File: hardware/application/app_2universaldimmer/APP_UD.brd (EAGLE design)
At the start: 87.1 x 67.3 mm, 94 parts, among them IC102 LM324N, IC2 LM324N, Q1 IRFP460, Q101 IRFP460, Q102 IRFP460, Q103 BC546B, Q104 MPSA44, Q2 IRFP460, Q3 BC546B, Q4 MPSA44

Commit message: Universaldimmer: V2.3 Klemme 101 versetzt
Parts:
- moved KL101 2.54 mm to (5.08, 25.4)
- moved L101 2.54 mm to (8.89, 6.35)
- moved R101 2.54 mm to (8.89, 15.2)
- moved F101 2.22 mm to (3.81, 11.7)
- moved V101 2.22 mm to (2.54, 18.1)
- moved C103 1.27 mm to (2.54, 3.81)
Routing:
- net N$26: track 53.0 -> 50.9 mm
- net N$75: track 17.6 -> 18.8 mm
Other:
- board text added: "2"
- board text added: "24"
- board text added: "25"
- board text added: "8"
- board text added: "9"
- board text added: "Universaldimmer V2.3 Freebus/petzi 15.1.2012"
- board text added: "V2.3"
- board text removed: "Universaldimmer V2.2 Freebus/petzi 5.1.2012"
- board text removed: "V2.2"

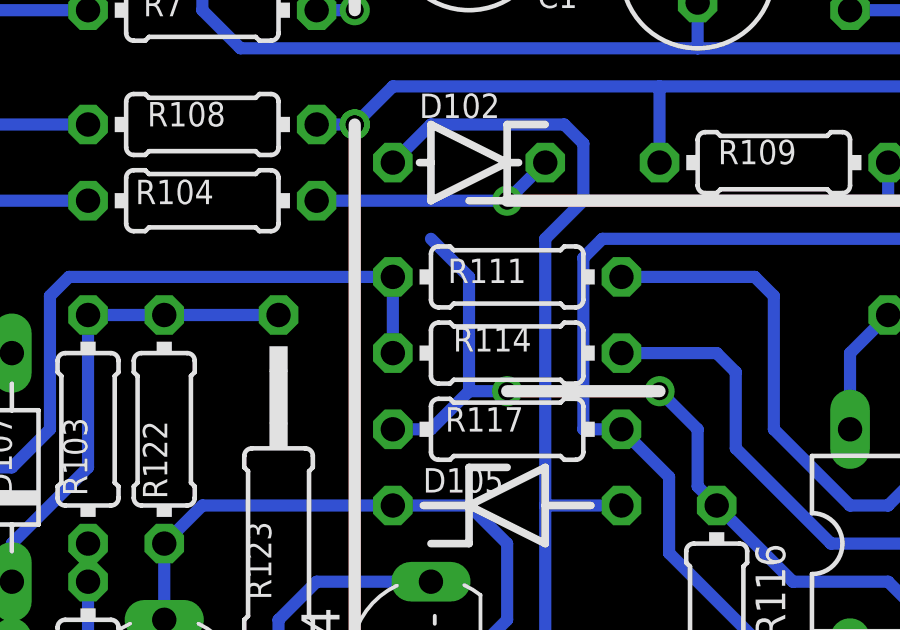
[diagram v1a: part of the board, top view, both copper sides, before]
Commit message: UD: unnötige Leiterbahn entfernt
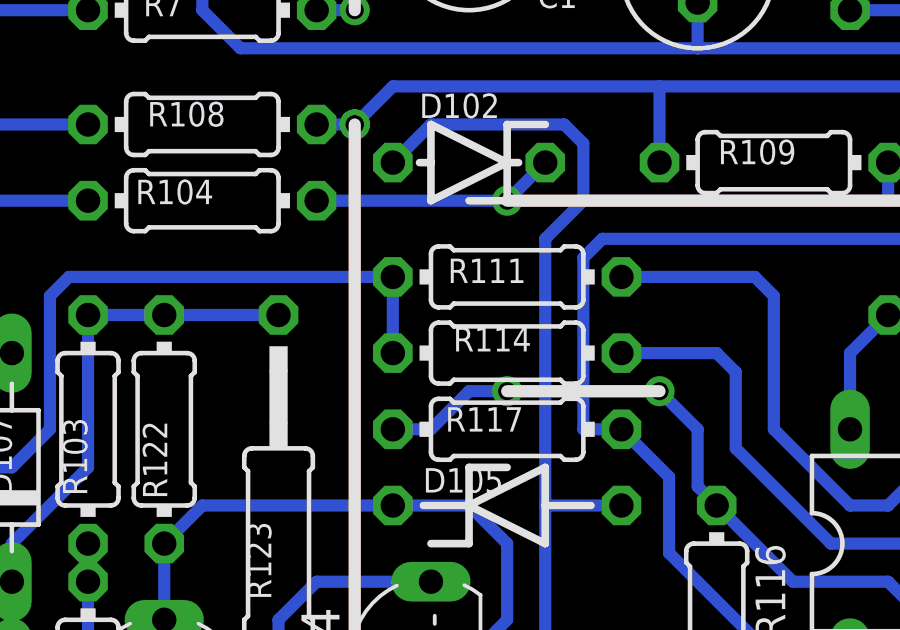
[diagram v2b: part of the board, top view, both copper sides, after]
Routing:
- net N$58: track 29.5 -> 23.8 mm
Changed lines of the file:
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@@
 <contactref element="R117" pad="2"/>
 <contactref element="IC102" pad="2"/>
-<wire x1="31.75" y1="27.94" x2="33.02" y2="26.67" width="0.4064" layer="16"/>
-<wire x1="33.02" y1="26.67" x2="33.02" y2="22.86" width="0.4064" layer="16"/>
 <wire x1="33.02" y1="22.86" x2="31.75" y2="21.59" width="0.4064" layer="16"/>
 <wire x1="31.75" y1="21.59" x2="30.48" y2="21.59" width="0.4064" layer="16"/>

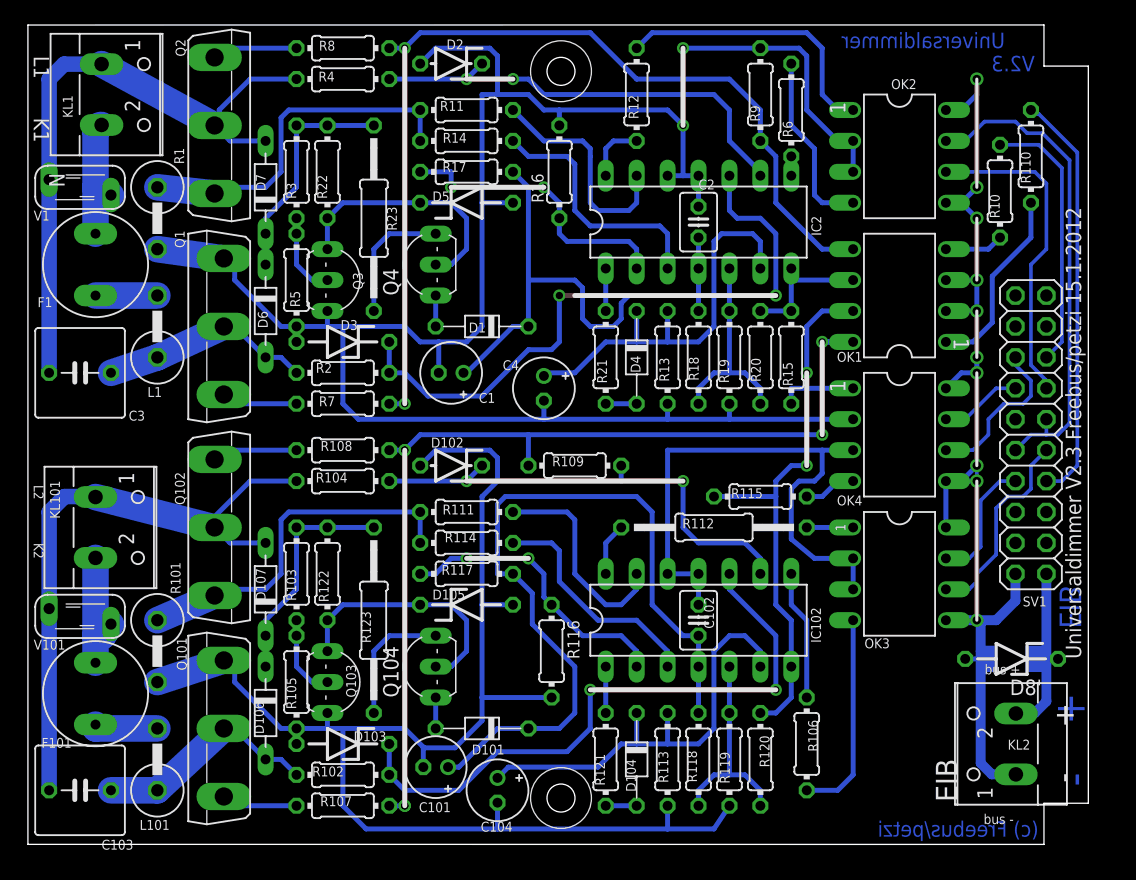
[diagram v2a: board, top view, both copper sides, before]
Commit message: Universaldimmer: V2.4  R23 nun 5Watt,deshalb Layout geändert, Schaltung ist gleich BOM und Warenkorb hinzugefügt
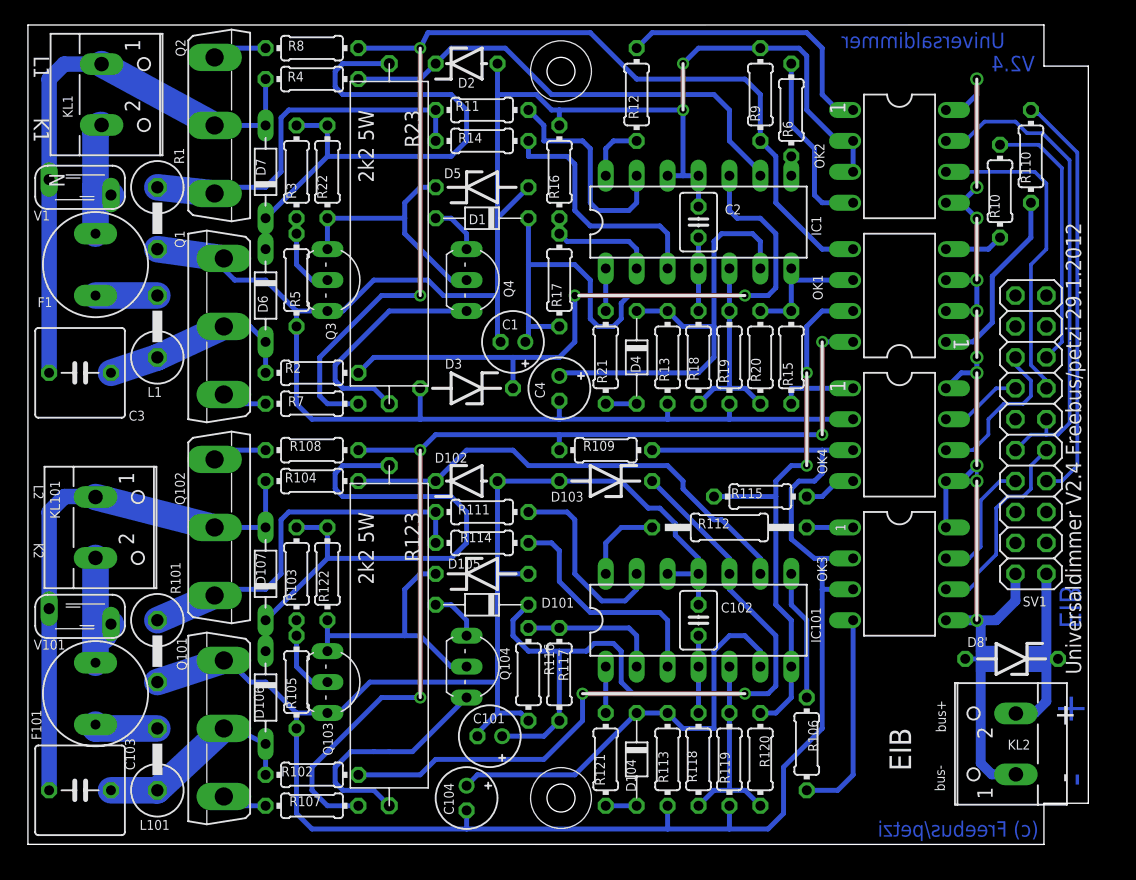
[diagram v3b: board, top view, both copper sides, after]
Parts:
- R109, R9: value 20k -> 22k
- R112: device rcl:0207/15 -> rcl:0207/12
- R123, R23: value 2k2 1W -> 2k2 5W; device rcl:0207/15 -> resistor-power:KH208-8_10B
- moved D103 30.5 mm to (45.7, 29.2)
- moved R17 11.7 mm to (41.9, 45.7), turned to 90 degrees
- moved R117 11.2 mm to (41.9, 13.3), turned to 90 degrees
- moved D3 10.9 mm to (34.3, 36.8)
- moved D101 10.2 mm to (35.6, 19.1)
- moved D1 8.89 mm to (35.6, 50.8)
- moved C1 5.68 mm to (38.1, 40.6)
- moved Q4 5.24 mm to (35.6, 45.7), turned to 270 degrees
- moved C101 5.12 mm to (36.2, 8.26)
- moved Q104 5.08 mm to (35.6, 14.0), turned to 270 degrees
- moved D105 2.84 mm to (35.6, 21.6)
- moved R109 2.84 mm to (45.7, 31.8)
- moved R116 2.69 mm to (39.4, 13.3)
- moved C104 2.62 mm to (34.3, 3.17)
- moved R102 2.54 mm to (21.6, 5.08)
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- renumbered IC102 to IC101, IC2 to IC1
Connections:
- net N$12: now also R23.P$1; no longer R23.1
- net N$35: now also R23.P$2; no longer R23.2
- net N$42: now also R123.P$1; no longer R123.1
- net N$63: now also R123.P$2; no longer R123.2
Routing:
- net N$42: track 18.8 -> 46.9 mm
- net V12-C2: track 66.4 -> 40.9 mm
- net N$12: track 21.4 -> 46.9 mm
- net AGND2: track 180.0 -> 194.8 mm
- net N$21: track 24.2 -> 9.73 mm, vias 2 -> 0
- net N$58: track 23.8 -> 11.7 mm, vias 2 -> 0
- net N$69: track 80.2 -> 90.5 mm
- net N$63: track 10.7 -> 19.7 mm
- net N$43: track 51.2 -> 59.7 mm
- net N$35: track 10.7 -> 19.1 mm
- net V12-C1: track 45.0 -> 38.8 mm
- net N$36: track 81.8 -> 87.9 mm
- net N$18: track 53.1 -> 48.0 mm
- net N$26: track 50.9 -> 46.2 mm
- net AGND1: track 177.1 -> 173.2 mm
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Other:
- board text added: "Universaldimmer V2.4 Freebus/petzi 29.1.2012"
- board text added: "V2.4"
- board text added: "bus+"
- board text added: "bus-"
- board text removed: "Universaldimmer V2.3 Freebus/petzi 15.1.2012"
- board text removed: "V2.3"
- board text removed: "bus +"
- board text removed: "bus -"
